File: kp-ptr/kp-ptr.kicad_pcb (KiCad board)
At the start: 4 copper layers, 31 x 101 mm, 171 parts, among them IC1 E22-900M22S, J1 ESP32_PROG_CON, J10 Conn_01x02, J11 Conn_01x02, J12 Conn_01x02, J13 Conn_01x02, J2 Conn_01x02, J3 Conn_01x02, J4 USB_C_Receptacle_USB2.0, J5 u.fl, J6 Conn_01x06_Male, J7 Conn_01x10_Male, J8 Conn_01x06_Male, J9 Conn_01x02_Male, Q1 NMOS_SOT23, Q2 DMC2025UFDB_v2, Q3 DMC2025UFDB_v2, Q4 DMC2025UFDB_v2, Q5 DMC2025UFDB_v2, U1 ESP32-S3FN8, U10 USBLC6-2SC6, U11 W25Q128JVS, U12 NL27WZU04DBVT1G, U2 MS560702BA03-50, U3 MMC5983MA, U4 H3LIS331, U5 L76-L, U6 NJG1156PCD, U7 LSM6DSO32, U8 AZ1117CH-5.0TRG1, U9 LDFM33PVR, Y1 7M40000005-40MHz

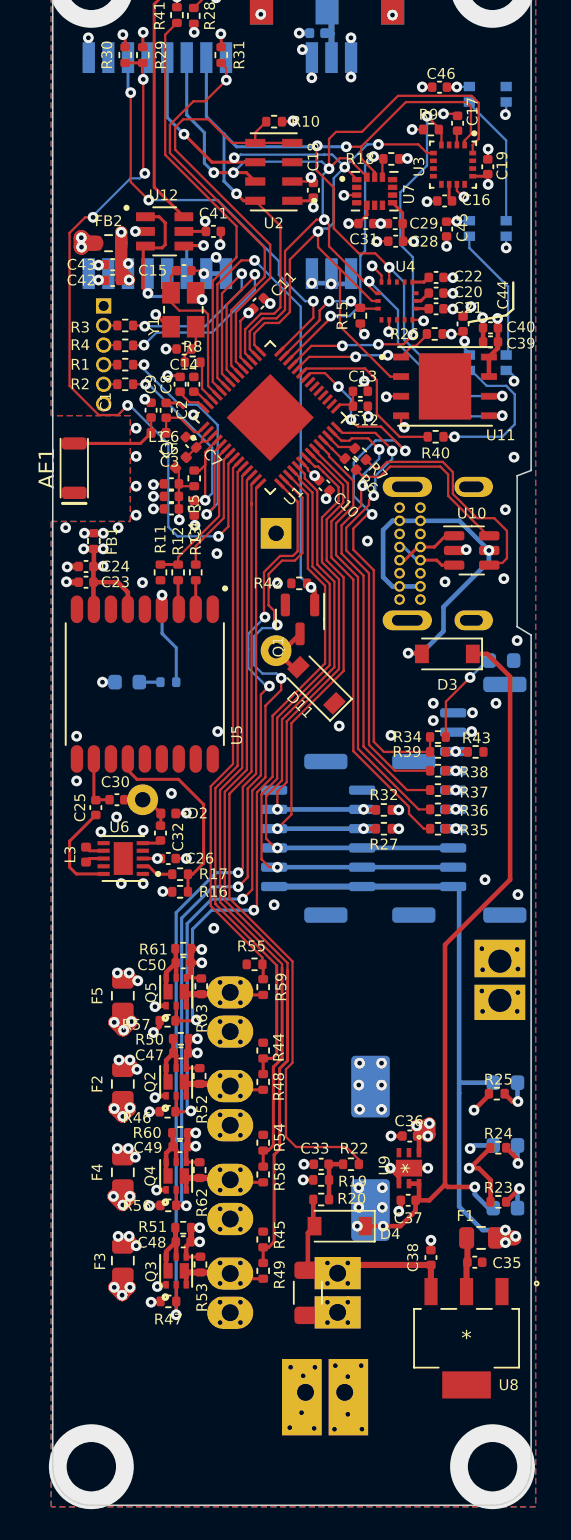
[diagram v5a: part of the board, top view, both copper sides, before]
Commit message: Next PCB update
-fixes
-logos added
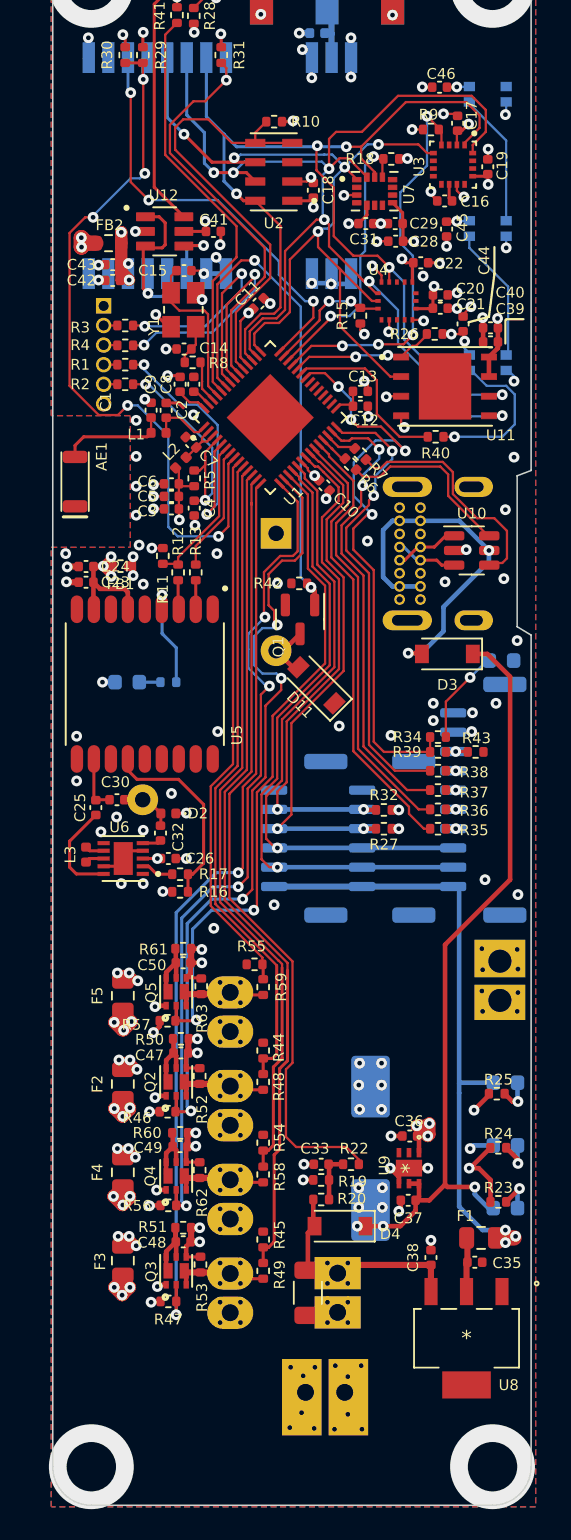
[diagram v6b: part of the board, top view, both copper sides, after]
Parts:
- added G***: LOGO, LOGO, B.Cu at (155.7, 60.7)
- added REF**: OSHW-Logo2_9.8x8mm_SilkScreen, Symbol:OSHW-Logo2_9.8x8mm_SilkScreen, B.Cu at (145.7, 67.0)
- moved FB1 2.37 mm to (145.5, 72.2), turned to 180 degrees
- moved C22 1.38 mm to (164.9, 52.6)
- moved R11 1.08 mm to (148.2, 71.6), turned to -90 degrees
- moved AE1 0.88 mm to (142.5, 66.8)
- moved C20 0.30 mm to (166.2, 54.7)
- moved C21 0.28 mm to (166.2, 55.5)
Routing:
- net Earth: track 71.6 -> 74.9 mm, vias 149 -> 150
- net +3V3: track 52.5 -> 55.5 mm, vias 27 -> 31
- net SPI_CLK: track 71.6 -> 72.4 mm
- net Net-(AE1-Pad2): track 6.15 -> 6.90 mm
- net +3.3VADC: track 10.9 -> 11.4 mm
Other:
- board text added: "PPS"
